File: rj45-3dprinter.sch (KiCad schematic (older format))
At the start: 11 parts, among them J1 ADXL, J2 FAN1, J3 8P8C, J4 FAN2, J5 E-MOTOR, J6 8P8C, J7 PROBE

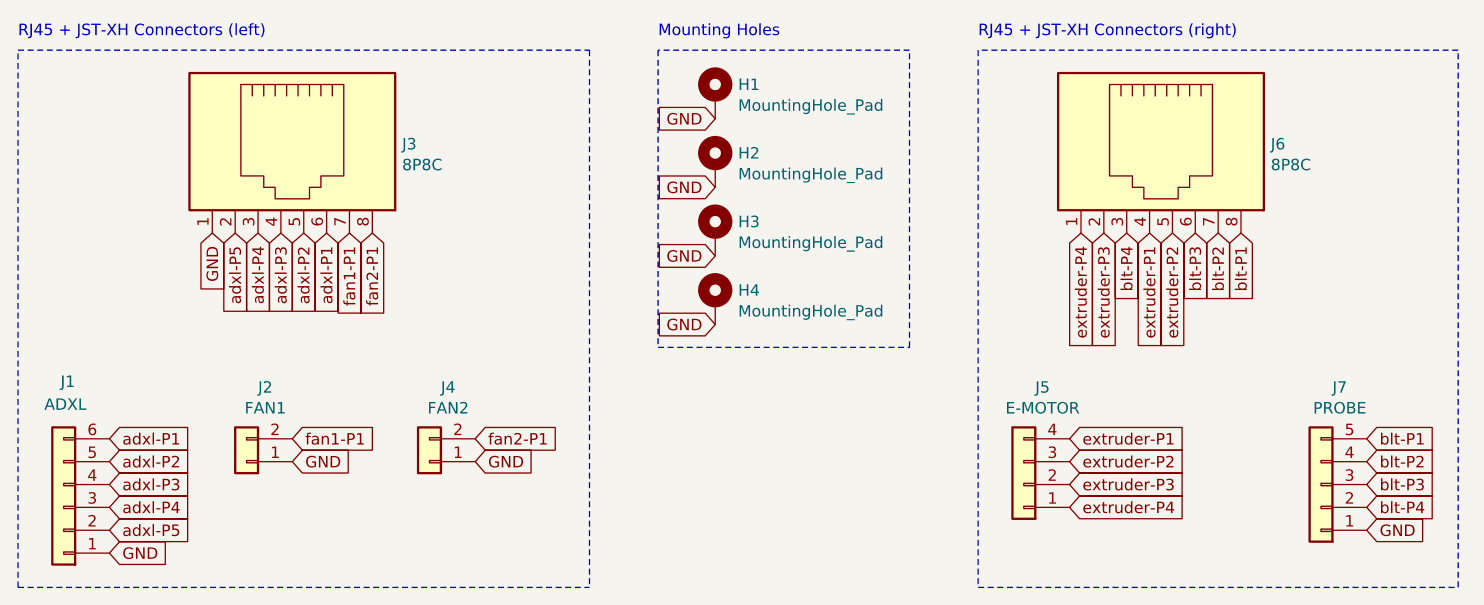
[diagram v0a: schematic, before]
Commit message: Update PCB for hotend (high-current) components
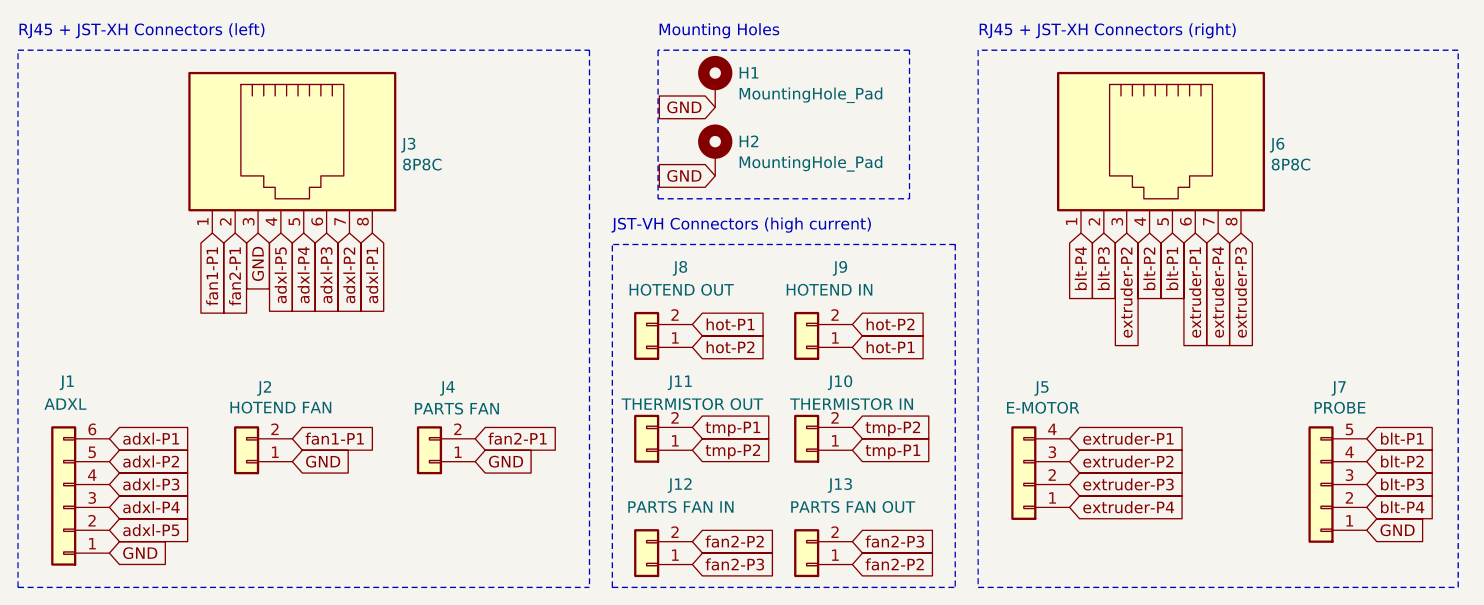
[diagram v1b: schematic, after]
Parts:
- removed H3, H4: MountingHole_Pad, MountingHole:MountingHole_3.2mm_M3_Pad_Via, symbol Mechanical:MountingHole_Pad
- added J10: THERMISTOR IN, Connector_JST:JST_VH_B2P-VH-FB-B_1x02_P3.96mm_Vertical, symbol Connector_Generic:Conn_01x02
- added J11: THERMISTOR OUT, Connector_JST:JST_VH_B2P-VH-FB-B_1x02_P3.96mm_Vertical, symbol Connector_Generic:Conn_01x02
- added J12: PARTS FAN IN, Connector_JST:JST_VH_B2P-VH-FB-B_1x02_P3.96mm_Vertical, symbol Connector_Generic:Conn_01x02
- added J13: PARTS FAN OUT, Connector_JST:JST_VH_B2P-VH-FB-B_1x02_P3.96mm_Vertical, symbol Connector_Generic:Conn_01x02
- added J8: HOTEND OUT, Connector_JST:JST_VH_B2P-VH-FB-B_1x02_P3.96mm_Vertical, symbol Connector_Generic:Conn_01x02
- added J9: HOTEND IN, Connector_JST:JST_VH_B2P-VH-FB-B_1x02_P3.96mm_Vertical, symbol Connector_Generic:Conn_01x02
- J2: value FAN1 -> HOTEND FAN
- J4: value FAN2 -> PARTS FAN
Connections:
- net GND: now also J3.3; no longer J3.1
- net adxl-P1: now also J3.8; no longer J3.6
- net adxl-P2: now also J3.7; no longer J3.5
- net adxl-P3: now also J3.6; no longer J3.4
- net adxl-P4: now also J3.5; no longer J3.3
- net adxl-P5: now also J3.4; no longer J3.2
- net blt-P1: now also J6.5; no longer J6.8
- net blt-P2: now also J6.4; no longer J6.7
- net blt-P3: now also J6.2; no longer J6.6
- net blt-P4: now also J6.1; no longer J6.3
- net extruder-P1: now also J6.6; no longer J6.4
- net extruder-P2: now also J6.3; no longer J6.5
- net extruder-P3: now also J6.8; no longer J6.2
- net extruder-P4: now also J6.7; no longer J6.1
- net fan1-P1: now also J3.1; no longer J3.7
- net fan2-P1: now also J3.2; no longer J3.8
- new net fan2-P2: J12.2 (Pin_2), J13.1 (Pin_1)
- new net fan2-P3: J12.1 (Pin_1), J13.2 (Pin_2)
- new net hot-P1: J8.2 (Pin_2), J9.1 (Pin_1)
- new net hot-P2: J8.1 (Pin_1), J9.2 (Pin_2)
- new net tmp-P1: J10.1 (Pin_1), J11.2 (Pin_2)
- new net tmp-P2: J10.2 (Pin_2), J11.1 (Pin_1)
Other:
- note added: "JST-VH Connectors (high current)"
- moved on the sheet: H1, H2
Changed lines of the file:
@@
 Sheet 1 1
 Title "μ3D: RatRig V-Core 3 EVA 2 wiring over RJ45"
-Date "2021-07-30"
-Rev "v.1"
+Date "2021-10-06"
+Rev "v.2"
 Comp "On-Prem"
 Comment1 "Author: aw"
@@
 Text GLabel 10600 5950 2    50   Input ~ 0
 blt-P4
+Text GLabel 9850 4750 3    50   Input ~ 0
+extruder-P1
+Text GLabel 9550 4750 3    50   Input ~ 0
+extruder-P2
+Text GLabel 9750 4750 3    50   Input ~ 0
+blt-P1
 Text GLabel 9650 4750 3    50   Input ~ 0
-extruder-P1
-Text GLabel 9750 4750 3    50   Input ~ 0
-extruder-P2
+blt-P2
+Text GLabel 9350 4750 3    50   Input ~ 0
+blt-P4
 Text GLabel 10050 4750 3    50   Input ~ 0
-blt-P1
-Text GLabel 9950 4750 3    50   Input ~ 0
-blt-P2
-Text GLabel 9550 4750 3    50   Input ~ 0
-blt-P4
+extruder-P3
 Text GLabel 9450 4750 3    50   Input ~ 0
-extruder-P3
-Text GLabel 9850 4750 3    50   Input ~ 0
 blt-P3
 $Comp
 L Mechanical:MountingHole_Pad H2
 U 1 1 61044D2D
-P 7750 4450
-F 0 "H2" H 7850 4499 50  0000 L CNN
-F 1 "MountingHole_Pad" H 7850 4408 50  0000 L CNN
-F 2 "MountingHole:MountingHole_3.2mm_M3_Pad_Via" H 7750 4450 50  0001 C CNN
-F 3 "~" H 7750 4450 50  0001 C CNN
-	1    7750 4450
+P 7750 4400
+F 0 "H2" H 7850 4449 50  0000 L CNN
+F 1 "MountingHole_Pad" H 7850 4358 50  0000 L CNN
+F 2 "MountingHole:MountingHole_3.2mm_M3_Pad_Via" H 7750 4400 50  0001 C CNN
+F 3 "~" H 7750 4400 50  0001 C CNN
+	1    7750 4400
 	1    0    0    -1
 $EndComp
@@
 L Mechanical:MountingHole_Pad H1
 U 1 1 61045123
-P 7750 4150
-F 0 "H1" H 7850 4199 50  0000 L CNN
-F 1 "MountingHole_Pad" H 7850 4108 50  0000 L CNN
-F 2 "MountingHole:MountingHole_3.2mm_M3_Pad_Via" H 7750 4150 50  0001 C CNN
-F 3 "~" H 7750 4150 50  0001 C CNN
-	1    7750 4150
+P 7750 4100
+F 0 "H1" H 7850 4149 50  0000 L CNN
+F 1 "MountingHole_Pad" H 7850 4058 50  0000 L CNN
+F 2 "MountingHole:MountingHole_3.2mm_M3_Pad_Via" H 7750 4100 50  0001 C CNN
+F 3 "~" H 7750 4100 50  0001 C CNN
+	1    7750 4100
 	1    0    0    -1
 $EndComp
-Text GLabel 7750 4550 0    50   Input ~ 0
-GND
-Text GLabel 7750 4250 0    50   Input ~ 0
+Text GLabel 7750 4500 0    50   Input ~ 0
+GND
+Text GLabel 7750 4200 0    50   Input ~ 0
 GND
 Text GLabel 9300 5950 2    50   Input ~ 0
 extruder-P4
-Text GLabel 9350 4750 3    50   Input ~ 0
+Text GLabel 9950 4750 3    50   Input ~ 0
 extruder-P4
-$Comp
-L Mechanical:MountingHole_Pad H3
-U 1 1 60FDE472
-P 7750 4750
-F 0 "H3" H 7850 4799 50  0000 L CNN
-F 1 "MountingHole_Pad" H 7850 4708 50  0000 L CNN
-F 2 "MountingHole:MountingHole_3.2mm_M3_Pad_Via" H 7750 4750 50  0001 C CNN
-F 3 "~" H 7750 4750 50  0001 C CNN
-	1    7750 4750
-	1    0    0    -1
-$EndComp
-$Comp
-L Mechanical:MountingHole_Pad H4
-U 1 1 60FDE7D4
-P 7750 5050
-F 0 "H4" H 7850 5099 50  0000 L CNN
-F 1 "MountingHole_Pad" H 7850 5008 50  0000 L CNN
-F 2 "MountingHole:MountingHole_3.2mm_M3_Pad_Via" H 7750 5050 50  0001 C CNN
-F 3 "~" H 7750 5050 50  0001 C CNN
-	1    7750 5050
-	1    0    0    -1
-$EndComp
-Text GLabel 7750 4850 0    50   Input ~ 0
-GND
-Text GLabel 7750 5150 0    50   Input ~ 0
-GND
-Wire Notes Line
-	8600 5250 8600 3950
 Wire Notes Line
 	8600 3950 7500 3950
 Wire Notes Line
-	7500 5250 8600 5250
-Wire Notes Line
-	7500 3950 7500 5250
+	7500 4600 8600 4600
 Text GLabel 6700 5750 2    50   Input ~ 0
 GND
 Text GLabel 6700 5650 2    50   Input ~ 0
 fan2-P1
-Text GLabel 6250 4750 3    50   Input ~ 0
+Text GLabel 5650 4750 3    50   Input ~ 0
 fan2-P1
-Text GLabel 6150 4750 3    50   Input ~ 0
+Text GLabel 5550 4750 3    50   Input ~ 0
 fan1-P1
 Text GLabel 5900 5750 2    50   Input ~ 0
@@
 Text GLabel 5100 6050 2    50   Input ~ 0
 adxl-P5
+Text GLabel 5950 4750 3    50   Input ~ 0
+adxl-P4
+Text GLabel 6050 4750 3    50   Input ~ 0
+adxl-P3
+Text GLabel 6150 4750 3    50   Input ~ 0
+adxl-P2
+Text GLabel 6250 4750 3    50   Input ~ 0
+adxl-P1
 Text GLabel 5750 4750 3    50   Input ~ 0
-adxl-P4
+GND
+Text GLabel 5100 6150 2    50   Input ~ 0
+GND
 Text GLabel 5850 4750 3    50   Input ~ 0
-adxl-P3
-Text GLabel 5950 4750 3    50   Input ~ 0
-adxl-P2
-Text GLabel 6050 4750 3    50   Input ~ 0
-adxl-P1
-Text GLabel 5550 4750 3    50   Input ~ 0
-GND
-Text GLabel 5100 6150 2    50   Input ~ 0
-GND
-Text GLabel 5650 4750 3    50   Input ~ 0
 adxl-P5
 Text GLabel 5100 5950 2    50   Input ~ 0
@@
 adxl-P1
 $Comp
-L Connector_Generic:Conn_01x02 J4
-U 1 1 60F945DF
-P 6500 5750
-F 0 "J4" H 6418 5425 50  0000 C CNN
-F 1 "FAN2" H 6418 5516 50  0000 C CNN
-F 2 "Connector_JST:JST_XH_B2B-XH-A_1x02_P2.50mm_Vertical" H 6500 5750 50  0001 C CNN
-F 3 "~" H 6500 5750 50  0001 C CNN
-	1    6500 5750
-	-1   0    0    1
-$EndComp
-$Comp
-L Connector_Generic:Conn_01x02 J2
-U 1 1 60F9425B
-P 5700 5750
-F 0 "J2" H 5618 5425 50  0000 C CNN
-F 1 "FAN1" H 5618 5516 50  0000 C CNN
-F 2 "Connector_JST:JST_XH_B2B-XH-A_1x02_P2.50mm_Vertical" H 5700 5750 50  0001 C CNN
-F 3 "~" H 5700 5750 50  0001 C CNN
-	1    5700 5750
-	-1   0    0    1
-$EndComp
-$Comp
 L Connector:8P8C J3
 U 1 1 60F903EA
@@
 Text Notes 8900 3900 0    50   ~ 0
 RJ45 + JST-XH Connectors (right)
+$Comp
+L Connector_Generic:Conn_01x02 J8
+U 1 1 615BE6D4
+P 7450 5250
+F 0 "J8" H 7300 4900 50  0000 C CNN
+F 1 "HOTEND OUT" H 7300 5000 50  0000 C CNN
+F 2 "Connector_JST:JST_VH_B2P-VH-FB-B_1x02_P3.96mm_Vertical" H 7450 5250 50  0001 C CNN
+F 3 "~" H 7450 5250 50  0001 C CNN
+	1    7450 5250
+	-1   0    0    1
+$EndComp
+Text GLabel 7650 5600 2    50   Input ~ 0
+tmp-P1
+Text GLabel 7650 5150 2    50   Input ~ 0
+hot-P1
+Text GLabel 8350 5700 2    50   Input ~ 0
+tmp-P1
+Text GLabel 7650 5250 2    50   Input ~ 0
+hot-P2
+Text GLabel 8350 5600 2    50   Input ~ 0
+tmp-P2
+Text GLabel 7650 5700 2    50   Input ~ 0
+tmp-P2
+$Comp
+L Connector_Generic:Conn_01x02 J2
+U 1 1 60F9425B
+P 5700 5750
+F 0 "J2" H 5618 5425 50  0000 C CNN
+F 1 "HOTEND FAN" H 5550 5515 50  0000 C CNN
+F 2 "Connector_JST:JST_XH_B2B-XH-A_1x02_P2.50mm_Vertical" H 5700 5750 50  0001 C CNN
+F 3 "~" H 5700 5750 50  0001 C CNN
+	1    5700 5750
+	-1   0    0    1
+$EndComp
+Text Notes 7300 4750 0    50   ~ 0
+JST-VH Connectors (high current)
+$Comp
+L Connector_Generic:Conn_01x02 J4
+U 1 1 60F945DF
+P 6500 5750
+F 0 "J4" H 6418 5425 50  0000 C CNN
+F 1 "PARTS FAN" H 6380 5520 50  0000 C CNN
+F 2 "Connector_JST:JST_XH_B2B-XH-A_1x02_P2.50mm_Vertical" H 6500 5750 50  0001 C CNN
+F 3 "~" H 6500 5750 50  0001 C CNN
+	1    6500 5750
+	-1   0    0    1
+$EndComp
+$Comp
+L Connector_Generic:Conn_01x02 J10
+U 1 1 615BEEDA
+P 8150 5700
+F 0 "J10" H 8000 5400 50  0000 C CNN
+F 1 "THERMISTOR IN" H 7950 5500 50  0000 C CNN
+F 2 "Connector_JST:JST_VH_B2P-VH-FB-B_1x02_P3.96mm_Vertical" H 8150 5700 50  0001 C CNN
+F 3 "~" H 8150 5700 50  0001 C CNN
+	1    8150 5700
+	-1   0    0    1
+$EndComp
+$Comp
+L Connector_Generic:Conn_01x02 J13
+U 1 1 616978E7
+P 8150 6200
+F 0 "J13" H 8000 5850 50  0000 C CNN
+F 1 "PARTS FAN OUT" H 7950 5950 50  0000 C CNN
+F 2 "Connector_JST:JST_VH_B2P-VH-FB-B_1x02_P3.96mm_Vertical" H 8150 6200 50  0001 C CNN
+F 3 "~" H 8150 6200 50  0001 C CNN
+	1    8150 6200
+	-1   0    0    1
+$EndComp
+Wire Notes Line
+	8800 4800 7300 4800
+Wire Notes Line
+	7300 6300 8800 6300
+Text GLabel 8350 5150 2    50   Input ~ 0
+hot-P2
+Text GLabel 8350 5250 2    50   Input ~ 0
+hot-P1
+$Comp
+L Connector_Generic:Conn_01x02 J9
+U 1 1 615CFC87
+P 8150 5250
+F 0 "J9" H 8000 4900 50  0000 C CNN
+F 1 "HOTEND IN" H 8050 5000 50  0000 C CNN
+F 2 "Connector_JST:JST_VH_B2P-VH-FB-B_1x02_P3.96mm_Vertical" H 8150 5250 50  0001 C CNN
+F 3 "~" H 8150 5250 50  0001 C CNN
+	1    8150 5250
+	-1   0    0    1
+$EndComp
+Text GLabel 8350 6100 2    50   Input ~ 0
+fan2-P3
+Text GLabel 8350 6200 2    50   Input ~ 0
+fan2-P2
+Text GLabel 7650 6100 2    50   Input ~ 0
+fan2-P2
+Text GLabel 7650 6200 2    50   Input ~ 0
+fan2-P3
+$Comp
+L Connector_Generic:Conn_01x02 J12
+U 1 1 61696BB7
+P 7450 6200
+F 0 "J12" H 7300 5850 50  0000 C CNN
+F 1 "PARTS FAN IN" H 7300 5950 50  0000 C CNN
+F 2 "Connector_JST:JST_VH_B2P-VH-FB-B_1x02_P3.96mm_Vertical" H 7450 6200 50  0001 C CNN
+F 3 "~" H 7450 6200 50  0001 C CNN
+	1    7450 6200
+	-1   0    0    1
+$EndComp
+$Comp
+L Connector_Generic:Conn_01x02 J11
+U 1 1 615DAAF7
+P 7450 5700
+F 0 "J11" H 7300 5400 50  0000 C CNN
+F 1 "THERMISTOR OUT" H 7250 5500 50  0000 C CNN
+F 2 "Connector_JST:JST_VH_B2P-VH-FB-B_1x02_P3.96mm_Vertical" H 7450 5700 50  0001 C CNN
+F 3 "~" H 7450 5700 50  0001 C CNN
+	1    7450 5700
+	-1   0    0    1
+$EndComp
+Wire Notes Line
+	8600 4600 8600 3950
+Wire Notes Line
+	7500 3950 7500 4600
+Wire Notes Line
+	8800 4800 8800 6300
+Wire Notes Line
+	7300 6300 7300 4800
 $EndSCHEMATC
